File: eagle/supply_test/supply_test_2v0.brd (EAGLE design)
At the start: 25.4 x 25.4 mm, 27 parts, among them J21 AC_INFILM, Q1 2N7002, U1 TPS62122

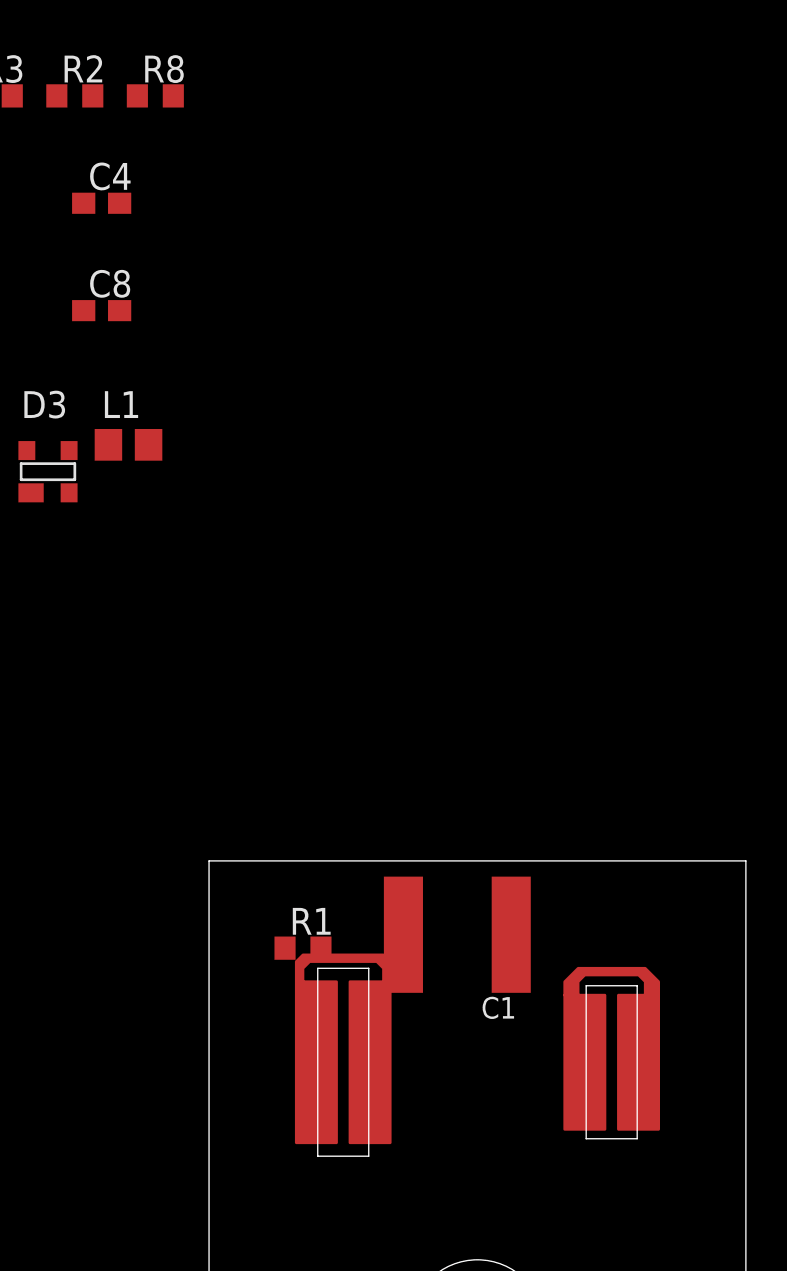
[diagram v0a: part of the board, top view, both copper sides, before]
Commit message: fixed flap layer issue
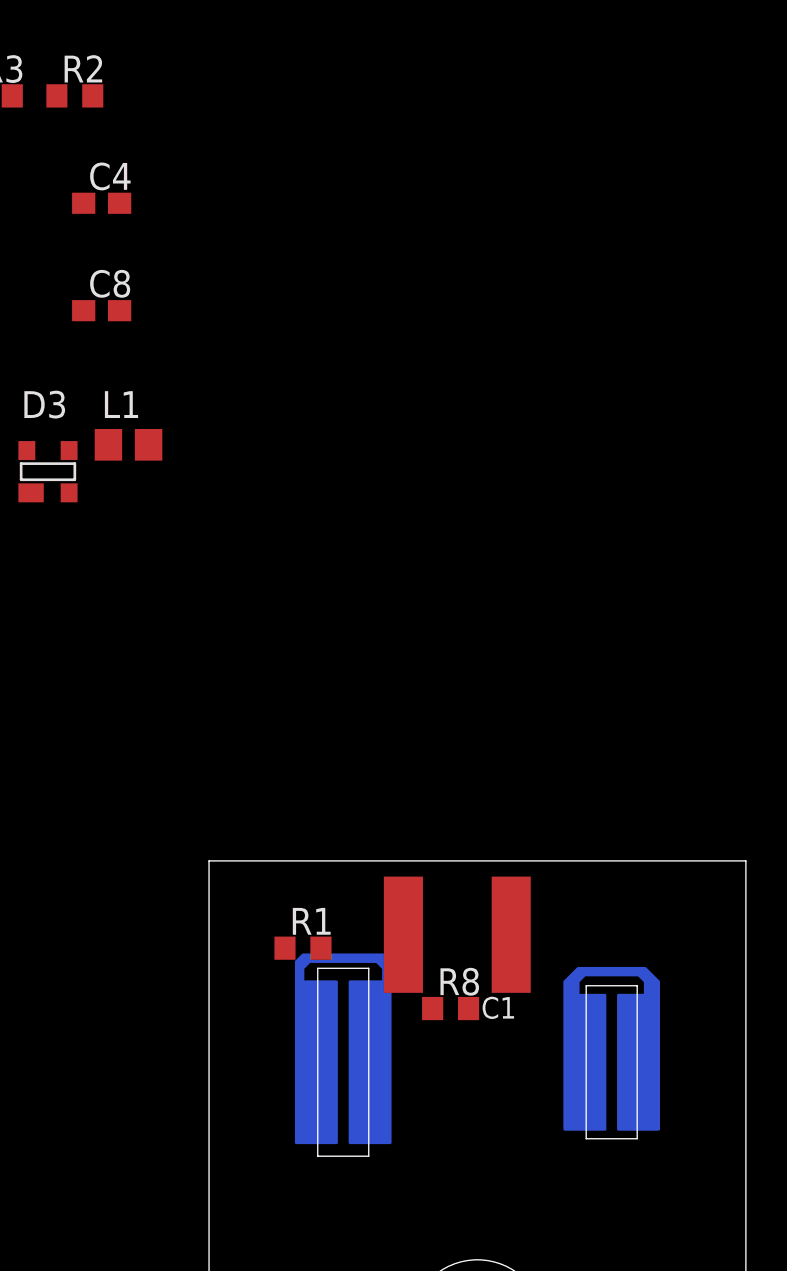
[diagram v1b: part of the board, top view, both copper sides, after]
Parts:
- moved R8 45.4 mm to (-1.27, 2.54)
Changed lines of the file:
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@@
 <layer number="23" name="tOrigins" color="15" fill="1" visible="yes" active="yes"/>
 <layer number="24" name="bOrigins" color="15" fill="1" visible="yes" active="yes"/>
-<layer number="25" name="tNames" color="7" fill="1" visible="yes" active="yes"/>
-<layer number="26" name="bNames" color="7" fill="1" visible="yes" active="yes"/>
-<layer number="27" name="tValues" color="7" fill="1" visible="yes" active="yes"/>
-<layer number="28" name="bValues" color="7" fill="1" visible="yes" active="yes"/>
+<layer number="25" name="tNames" color="7" fill="1" visible="no" active="yes"/>
+<layer number="26" name="bNames" color="7" fill="1" visible="no" active="yes"/>
+<layer number="27" name="tValues" color="7" fill="1" visible="no" active="yes"/>
+<layer number="28" name="bValues" color="7" fill="1" visible="no" active="yes"/>
 <layer number="29" name="tStop" color="7" fill="3" visible="no" active="yes"/>
 <layer number="30" name="bStop" color="7" fill="6" visible="no" active="yes"/>
@@
 <attribute name="DIGIKEY" value="BGX50AINCT-ND" x="0" y="0" size="1.778" layer="27" display="off"/>
 </element>
-<element name="R8" library="rcl" package="R0603" value="1M" x="-15.24" y="45.72">
-<attribute name="DIGIKEY" value="MCT0603-1.00M-CFCT-ND" x="0" y="0" size="1.778" layer="27" display="off"/>
+<element name="R8" library="rcl" package="R0603" value="1M" x="-1.27" y="2.54">
+<attribute name="DIGIKEY" value="MCT0603-1.00M-CFCT-ND" x="13.97" y="-43.18" size="1.778" layer="27" display="off"/>
 </element>
 <element name="U1" library="powerfilm" package="WDFN-6" value="TPS62122" x="-26.67" y="44.45">
@@
 <contactref element="R8" pad="1"/>
 <wire x1="-7.405" y1="5.3975" x2="-3.5025" y2="6.0325" width="0" layer="19" extent="1-1"/>
-<wire x1="-16.09" y1="45.72" x2="-7.405" y2="5.3975" width="0" layer="19" extent="1-1"/>
+<wire x1="-2.12" y1="2.54" x2="-7.405" y2="5.3975" width="0" layer="19" extent="1-1"/>
 </signal>
 <signal name="N$2">
@@
 <wire x1="-36.41" y1="40.64" x2="1.5975" y2="6.0325" width="0" layer="19" extent="1-1"/>
 <wire x1="-19.9" y1="45.72" x2="-36.41" y2="40.64" width="0" layer="19" extent="1-1"/>
-<wire x1="-14.39" y1="45.72" x2="-19.9" y2="45.72" width="0" layer="19" extent="1-1"/>
+<wire x1="-0.42" y1="2.54" x2="-19.9" y2="45.72" width="0" layer="19" extent="1-1"/>
 </signal>
 <signal name="N$5">

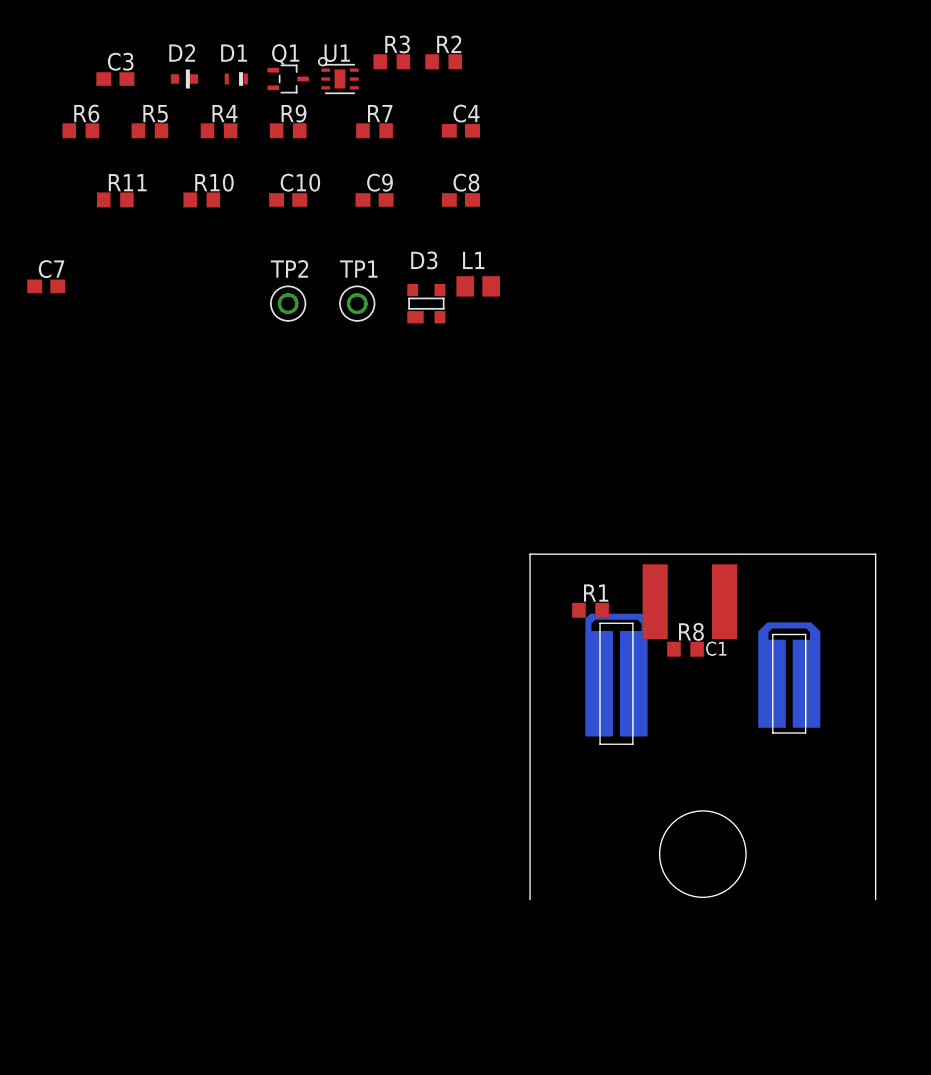
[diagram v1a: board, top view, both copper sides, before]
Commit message: re-arranged full wave and enable
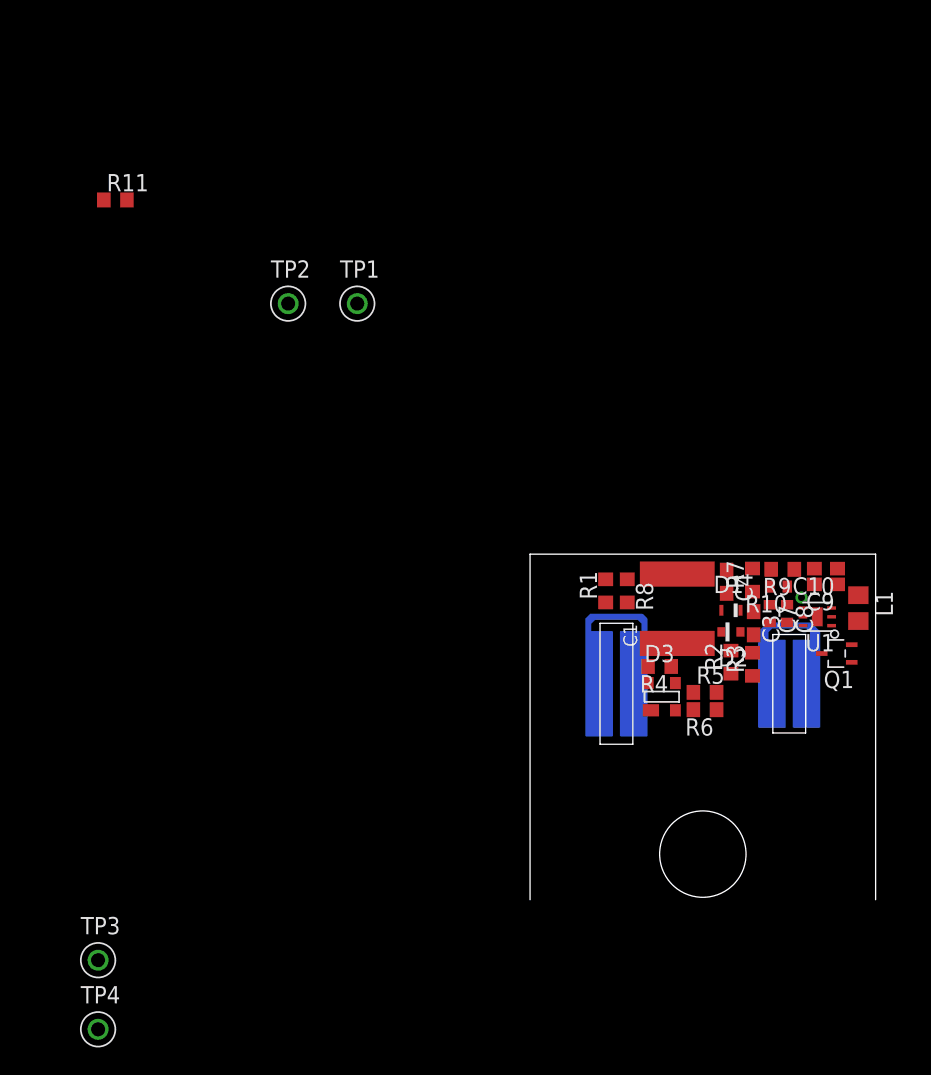
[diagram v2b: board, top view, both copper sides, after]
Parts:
- added TP3, TP4: TP_STD, skyspecs:TP
- C7, C8: device rcl:C0603 -> rcl:C0402
- R10: device rcl:R0603 -> rcl:R0402
- moved R6 62.6 mm to (0.16, -1.91), turned to 180 degrees
- moved C3 61.7 mm to (3.73, 4.45), turned to 270 degrees
- moved Q1 58.4 mm to (9.84, 2.22), turned to 180 degrees
- moved C7 58.4 mm to (4.92, 5.16), turned to 270 degrees
- moved R5 58.0 mm to (0.16, -0.64)
- moved D2 57.1 mm to (2.06, 3.81), turned to 180 degrees
- moved D1 53.4 mm to (2.06, 5.40)
- moved U1 52.9 mm to (8.41, 4.92), turned to 180 degrees
- moved R3 51.6 mm to (3.65, 1.43), turned to 90 degrees
- moved R10 51.0 mm to (5.56, 7.14), turned to 180 degrees
- moved R4 51.0 mm to (-3.17, 1.27), turned to 180 degrees
- moved R2 48.9 mm to (2.06, 1.59), turned to 90 degrees
- moved R9 48.6 mm to (5.87, 8.41), turned to 180 degrees
- moved C10 47.9 mm to (9.05, 8.46), turned to 180 degrees
- moved C9 43.6 mm to (9.05, 7.30), turned to 180 degrees
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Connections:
- net +3V3: now also TP4.P$1
- net N$1: now also TP3.P$1

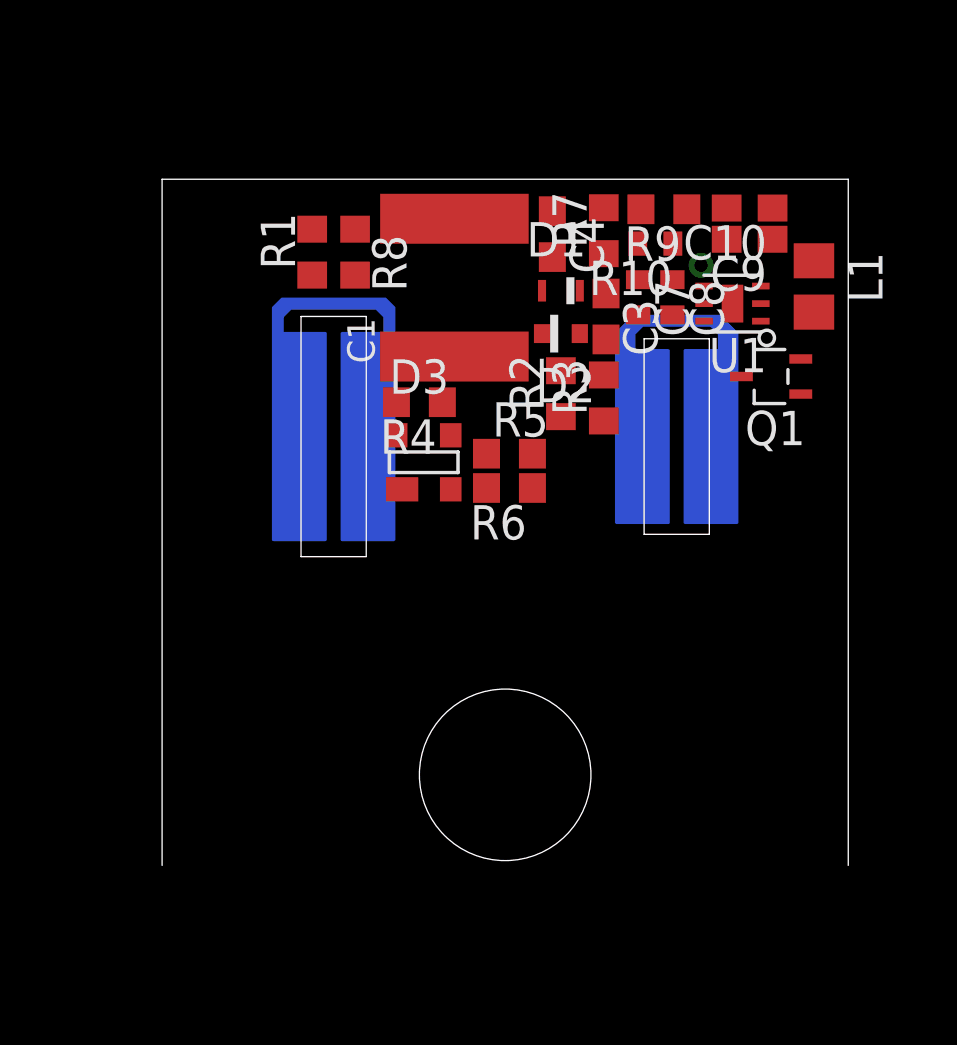
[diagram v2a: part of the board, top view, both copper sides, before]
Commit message: finalized three prong placement
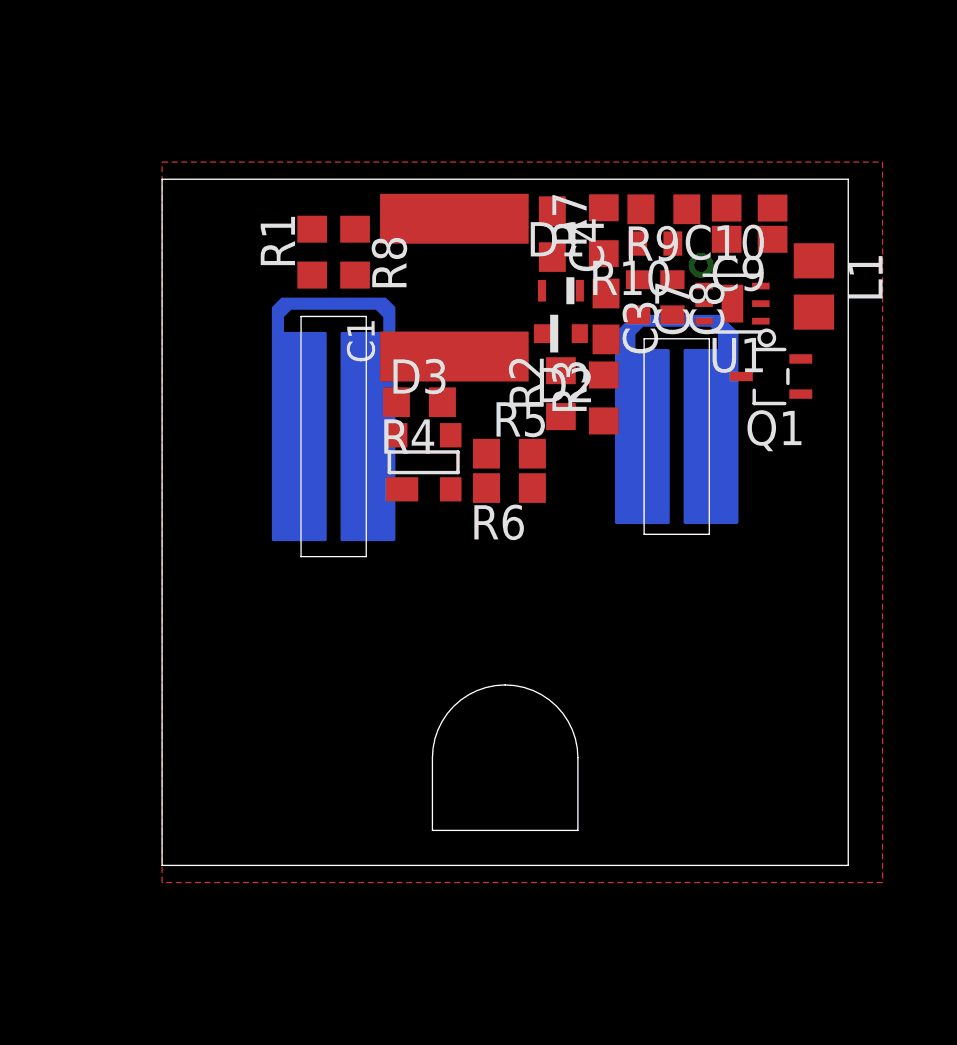
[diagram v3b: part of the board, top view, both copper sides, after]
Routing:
- added copper zone on layer 1, net GND
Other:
- outline, holes or cut-outs redrawn
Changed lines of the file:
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@@
 <contactref element="D2" pad="C"/>
 <contactref element="R2" pad="2"/>
-<wire x1="2.06375" y1="2.4375" x2="1.36375" y2="5.3975" width="0" layer="19" extent="1-1"/>
-<wire x1="1.36375" y1="3.81" x2="2.06375" y2="2.4375" width="0" layer="19" extent="1-1"/>
+<wire x1="1.36375" y1="3.81" x2="1.36375" y2="5.3975" width="0" layer="19" extent="1-1"/>
+<wire x1="2.06375" y1="2.4375" x2="1.36375" y2="3.81" width="0" layer="19" extent="1-1"/>
 </signal>
 <signal name="GND">
@@
 <contactref element="C9" pad="2"/>
 <contactref element="C10" pad="2"/>
-<wire x1="8.19875" y1="7.3025" x2="6.72375" y2="8.41375" width="0" layer="19" extent="1-1"/>
-<wire x1="8.19875" y1="8.4582" x2="8.19875" y2="7.3025" width="0" layer="19" extent="1-1"/>
-<wire x1="8.41375" y1="4.92125" x2="8.19875" y2="7.3025" width="0" layer="19" extent="1-1"/>
-<wire x1="7.36375" y1="4.27125" x2="8.41375" y2="4.92125" width="0" layer="19" extent="1-1"/>
+<polygon width="0.4064" layer="1">
+<vertex x="-12.7" y="10.16"/>
+<vertex x="13.97" y="10.16"/>
+<vertex x="13.97" y="-16.51"/>
+<vertex x="-12.7" y="-16.51"/>
+</polygon>
 <wire x1="6.19125" y1="4.5062" x2="7.36375" y2="4.27125" width="0" layer="19" extent="1-1"/>
-<wire x1="4.92125" y1="4.5062" x2="6.19125" y2="4.5062" width="0" layer="19" extent="1-1"/>
-<wire x1="-2.01625" y1="0.0475" x2="4.92125" y2="4.5062" width="0" layer="19" extent="1-1"/>
+<wire x1="8.41375" y1="4.92125" x2="7.36375" y2="4.27125" width="0" layer="19" extent="1-1"/>
+<wire x1="3.7338" y1="3.595" x2="4.92125" y2="4.5062" width="0" layer="19" extent="1-1"/>
+<wire x1="2.76375" y1="3.81" x2="3.7338" y2="3.595" width="0" layer="19" extent="1-1"/>
 <wire x1="-30.48" y1="27.94" x2="-2.01625" y2="0.0475" width="0" layer="19" extent="1-1"/>
 <wire x1="-42.33" y1="35.56" x2="-30.48" y2="27.94" width="0" layer="19" extent="1-1"/>
-<wire x1="3.7338" y1="3.595" x2="-42.33" y2="35.56" width="0" layer="19" extent="1-1"/>
-<wire x1="2.76375" y1="3.81" x2="3.7338" y2="3.595" width="0" layer="19" extent="1-1"/>
-<wire x1="10.9425" y1="2.8725" x2="2.76375" y2="3.81" width="0" layer="19" extent="1-1"/>
 </signal>
 <signal name="VCC">
@@
 <contactref element="C7" pad="1"/>
 <wire x1="4.92125" y1="5.8062" x2="6.19125" y2="5.8062" width="0" layer="19" extent="1-1"/>
+<wire x1="3.7338" y1="5.295" x2="4.92125" y2="5.8062" width="0" layer="19" extent="1-1"/>
+<wire x1="2.76375" y1="5.3975" x2="3.7338" y2="5.295" width="0" layer="19" extent="1-1"/>
+<wire x1="4.90625" y1="7.14375" x2="4.92125" y2="5.8062" width="0" layer="19" extent="1-1"/>
 <wire x1="7.36375" y1="4.92125" x2="6.19125" y2="5.8062" width="0" layer="19" extent="1-1"/>
-<wire x1="2.76375" y1="5.3975" x2="7.36375" y2="4.92125" width="0" layer="19" extent="1-1"/>
-<wire x1="3.65125" y1="2.27875" x2="2.76375" y2="5.3975" width="0" layer="19" extent="1-1"/>
-<wire x1="-25.4" y1="27.94" x2="4.92125" y2="5.8062" width="0" layer="19" extent="1-1"/>
-<wire x1="4.90625" y1="7.14375" x2="-25.4" y2="27.94" width="0" layer="19" extent="1-1"/>
-<wire x1="1.00875" y1="-0.635" x2="4.90625" y2="7.14375" width="0" layer="19" extent="1-1"/>
-<wire x1="3.7338" y1="5.295" x2="1.00875" y2="-0.635" width="0" layer="19" extent="1-1"/>
+<wire x1="3.65125" y1="2.27875" x2="3.7338" y2="5.295" width="0" layer="19" extent="1-1"/>
+<wire x1="1.00875" y1="-0.635" x2="3.65125" y2="2.27875" width="0" layer="19" extent="1-1"/>
+<wire x1="-25.4" y1="27.94" x2="2.76375" y2="5.3975" width="0" layer="19" extent="1-1"/>
 </signal>
 <signal name="N$4">
@@
 <contactref element="R4" pad="1"/>
 <contactref element="R2" pad="1"/>
-<wire x1="-1.8796" y1="2.9618" x2="2.06375" y2="0.7375" width="0" layer="19" extent="1-1"/>
+<wire x1="-2.325" y1="1.27" x2="-1.8796" y2="2.9618" width="0" layer="19" extent="1-1"/>
+<wire x1="2.06375" y1="0.7375" x2="-2.325" y2="1.27" width="0" layer="19" extent="1-1"/>
 <wire x1="-5.55625" y1="5.97625" x2="-1.8796" y2="2.9618" width="0" layer="19" extent="1-1"/>
-<wire x1="-2.325" y1="1.27" x2="-1.8796" y2="2.9618" width="0" layer="19" extent="1-1"/>
 </signal>
 <signal name="N$5">
@@
 <contactref element="R6" pad="2"/>
 <contactref element="D3" pad="P2"/>
-<wire x1="-0.69125" y1="-1.905" x2="-2.01625" y2="-1.9525" width="0" layer="19" extent="1-1"/>
+<wire x1="-2.01625" y1="-1.9525" x2="-0.69125" y2="-1.905" width="0" layer="19" extent="1-1"/>
 </signal>
 <signal name="N$13">
@@
 <contactref element="R9" pad="2"/>
 <contactref element="C4" pad="2"/>
-<wire x1="5.02375" y1="8.41375" x2="1.74625" y2="6.643" width="0" layer="19" extent="1-1"/>
-<wire x1="9.46375" y1="5.57125" x2="5.02375" y2="8.41375" width="0" layer="19" extent="1-1"/>
+<wire x1="5.02375" y1="8.41375" x2="9.46375" y2="5.57125" width="0" layer="19" extent="1-1"/>
 <wire x1="3.65125" y1="6.77" x2="5.02375" y2="8.41375" width="0" layer="19" extent="1-1"/>
+<wire x1="1.74625" y1="6.643" x2="3.65125" y2="6.77" width="0" layer="19" extent="1-1"/>
 </signal>
 <signal name="N$16">
